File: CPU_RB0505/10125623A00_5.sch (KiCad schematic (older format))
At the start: 46 parts, among them IC21 LT1236ACS8-5, IC23 LT1236ACS8-10, IC24 STM809LWX, IC25 STM809LWX, IC26 LF33CDT, IC29 TPS5430, IC36 STM809TWX, T10 FZT953, T11 FZT953, T12 FZT953

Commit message: Sheet 5 made on grid and "pretty"
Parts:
- removed C46, C74, C80, C83: 100nF, 10125623A00:C0805, symbol 10125623A00-eagle-import:C0805
- removed C47: 220pF, 10125623A00:C0805, symbol 10125623A00-eagle-import:C0805
- removed D11: STPS340U, 10125623A00:SOT23DIO, symbol 10125623A00-eagle-import:BAT54
- removed IC29: TPS5430, 10125623A00:SO8POWERPAD, symbol 10125623A00-eagle-import:TPS5430DDA
- removed L2: 33µH, 10125623A00:WE-TPC-MH, symbol 10125623A00-eagle-import:WE-TPC-MH
- removed L30: 7427504, 10125623A00:PERL-FER, symbol 10125623A00-eagle-import:7427504
- removed R36: 75K, 10125623A00:R0805, symbol 10125623A00-eagle-import:R0805
- removed R41: 4.7K, 10125623A00:R1206, symbol 10125623A00-eagle-import:R1206
- removed T12: FZT953, 10125623A00:SOT223, symbol 10125623A00-eagle-import:BCP51
- added C117: 10µF, 10125623A00:TANTALB, symbol cpu-board:TANTALB
- added C80 (x2): 100nF, 10125623A00:C0805, symbol 10125623A00-eagle-import:C0805
- added C81: 10uF, 10125623A00:TANTALD, symbol cpu-board:TANTALD
- added D11 (x2): STPS340U, 10125623A00:SOT23DIO, symbol 10125623A00-eagle-import:BAT54
- added IC29 (x2): TPS5430, 10125623A00:SO8POWERPAD, symbol 10125623A00-eagle-import:TPS5430DDA
- added L2 (x2): 33µH, 10125623A00:WE-TPC-MH, symbol 10125623A00-eagle-import:WE-TPC-MH
- added T12 (x2): FZT953, 10125623A00:SOT223, symbol 10125623A00-eagle-import:BCP51
- C106: symbol 10125623A00-eagle-import:CHCMS_D8 -> cpu-board:CHCMS_D8
- C108, C92: symbol 10125623A00-eagle-import:TANTALB -> cpu-board:TANTALB
- C21, C88: symbol 10125623A00-eagle-import:MV100?F50V -> cpu-board:MV100?F50V
- C85: symbol 10125623A00-eagle-import:TANTALD -> cpu-board:TANTALD
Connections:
- wire segments 181 -> 180
- no-connect marks 0 -> 3

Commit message: Combined all symbols into one project library
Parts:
- C105, C107, C79, C80, C82, C90, C91, C97: symbol 10125623A00-eagle-import:C0805 -> cpu-board:C0805
- C117: symbol 10125623A00-eagle-import:TANTALB -> cpu-board:TANTALB
- C81: symbol 10125623A00-eagle-import:TANTALD -> cpu-board:TANTALD
- D11: symbol 10125623A00-eagle-import:BAT54 -> cpu-board:BAT54
- D4: symbol 10125623A00-eagle-import:ICTE5 -> cpu-board:ICTE5
- D7: symbol 10125623A00-eagle-import:PRLL5819 -> cpu-board:PRLL5819
- FU2: symbol 10125623A00-eagle-import:SLOBLO -> cpu-board:SLOBLO
- IC21, IC23: symbol 10125623A00-eagle-import:LT1236 -> cpu-board:LT1236
- IC24, IC25, IC36: symbol 10125623A00-eagle-import:STM809 -> cpu-board:STM809
- IC26: symbol 10125623A00-eagle-import:LF33CDT -> cpu-board:LF33CDT
- IC29: symbol 10125623A00-eagle-import:TPS5430DDA -> cpu-board:TPS5430DDA
- JP9: symbol 10125623A00-eagle-import:JUMP_0U -> cpu-board:JUMP_0U
- L2: symbol 10125623A00-eagle-import:WE-TPC-MH -> cpu-board:WE-TPC-MH
- R35, R40, R44, R66, R67, R71, R73: symbol 10125623A00-eagle-import:R0805 -> cpu-board:R0805
- T10, T11, T12: symbol 10125623A00-eagle-import:BCP51 -> cpu-board:BCP51
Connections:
- wire segments 180 -> 177
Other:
- moved on the sheet: C117

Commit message: Corrected merge errors on sheet 5
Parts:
- removed C117 (x2): 10µF, 10125623A00:TANTALB, symbol cpu-board:TANTALB
- removed C80 (x2): 100nF, 10125623A00:C0805, symbol cpu-board:C0805
- removed C81 (x2): 10uF, 10125623A00:TANTALD, symbol cpu-board:TANTALD
- removed D11 (x2): STPS340U, 10125623A00:SOT23DIO, symbol cpu-board:BAT54
- removed IC29 (x2): TPS5430, 10125623A00:SO8POWERPAD, symbol cpu-board:TPS5430DDA
- removed L2 (x2): 33µH, 10125623A00:WE-TPC-MH, symbol cpu-board:WE-TPC-MH
- removed T12 (x2): FZT953, 10125623A00:SOT223, symbol cpu-board:BCP51
- added 1: CART_A3, symbol cpu-board:CART_A3
- added C117: 10µF, 10125623A00:TANTALB, symbol cpu-board:TANTALB
- added C46, C74, C80, C83: 100nF, 10125623A00:C0805, symbol cpu-board:C0805
- added C47: 220pF, 10125623A00:C0805, symbol cpu-board:C0805
- added C81: 10uF, 10125623A00:TANTALD, symbol cpu-board:TANTALD
- added D11: STPS340U, 10125623A00:SOT23DIO, symbol cpu-board:BAT54
- added IC29: TPS5430, 10125623A00:SO8POWERPAD, symbol cpu-board:TPS5430DDA
- added L2: 33µH, 10125623A00:WE-TPC-MH, symbol cpu-board:WE-TPC-MH
- added L30: 7427504, 10125623A00:PERL-FER, symbol cpu-board:7427504
- added R36: 75K, 10125623A00:R0805, symbol cpu-board:R0805
- added R41: 4.7K, 10125623A00:R1206, symbol cpu-board:R1206
- added T12: FZT953, 10125623A00:SOT223, symbol cpu-board:BCP51
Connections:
- net labels removed: CART_A3, PORT, PORT_LONG
- wire segments 177 -> 178
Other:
- moved on the sheet: C117, C21, IC21, IC23

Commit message: Sheet 5 labels converted to hier.
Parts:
- removed 1: CART_A3, symbol cpu-board:CART_A3
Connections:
- net +10VREF: no longer names the net of C83.2, C85.+, IC23.6 (OUT), T12.2 (C), T12.4 (C2)
- net +10VREF: no longer R66.1
- net +3,3V: no longer names the net of C90.2, C92.+, IC26.OUTPUT (VOUT)
- net +3,3V: no longer IC36.3 (VCC)
- net +5VREF: no longer names the net of C80.2, C81.+, IC21.6 (OUT), T11.2 (C), T11.4 (C2)
- net +5VREF: no longer IC24.3 (VCC)
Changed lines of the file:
@@
 Text Notes 13825 11025 0    170  ~ 0
 10125623
-Text GLabel 4175 2250 2    56   Output ~ 0
-+5VREF
-Text GLabel 4175 4650 2    56   Output ~ 0
-+10VREF
-Text GLabel 4250 6400 2    56   Output ~ 0
-+3,3V
-Text GLabel 7850 3900 0    56   Input ~ 0
-+10VREF
-Text GLabel 7850 6250 0    70   Input ~ 0
-+3,3V
-Text GLabel 9825 2300 2    56   Output ~ 0
+Text HLabel 9825 2300 2    56   Output ~ 0
 +5VREF-FAILURE
-Text GLabel 9825 4575 2    56   Output ~ 0
+Text HLabel 9825 4575 2    56   Output ~ 0
 +10VREF-FAILURE
-Text GLabel 9825 6925 2    56   Output ~ 0
+Text HLabel 9825 6925 2    56   Output ~ 0
 +3,3V-FAILURE
-Text GLabel 15250 2500 2    56   Output ~ 0
+Text HLabel 15250 2500 2    56   Output ~ 0
 MES-24V
 $Comp
@@
 Connection ~ 3925 2250
 Wire Wire Line
-	3925 2250 4175 2250
-Wire Wire Line
 	3925 2375 3925 2250
 Wire Wire Line
@@
 Connection ~ 3925 4650
 Wire Wire Line
-	3925 4650 4175 4650
-Wire Wire Line
 	3925 4775 3925 4650
 Wire Wire Line
@@
 Wire Wire Line
 	3975 6250 3975 6400
-Connection ~ 3975 6400
-Wire Wire Line
-	3975 6400 4250 6400
 Wire Wire Line
 	1700 9875 1700 10325
@@
 Wire Wire Line
 	7950 3900 7850 3900
-Text GLabel 7850 1625 0    56   Input ~ 0
-+5VREF
-Wire Wire Line
-	7850 1625 8750 1625
-Wire Wire Line
-	8750 1625 8750 1800
+Wire Wire Line
+	7850 1750 8750 1750
+Wire Wire Line
+	8750 1750 8750 1800
 Wire Wire Line
 	9450 2300 9825 2300
@@
 	12700 1975 12975 1975
 $Comp
-L cpu-board:CART_A3 1
-U 1 1 5EBB773C
-P 925 11100
-F 0 "1" H 975 11150 50  0001 C CNN
-F 1 "CART_A3" H 925 11100 50  0001 C CNN
-F 2 "" H 925 11100 50  0001 C CNN
-F 3 "" H 925 11100 50  0001 C CNN
-	1    925  11100
-	1    0    0    -1
-$EndComp
+L cpu-board:+3,3V #U$?
+U 1 1 5E9E0DC3
+P 7850 6300
+AR Path="/5E9E0DC3" Ref="#U$?"  Part="1"
+AR Path="/5E92540F/5E9E0DC3" Ref="#U$?"  Part="1"
+F 0 "#U$?" H 7850 6300 50  0001 C CNN
+F 1 "+3,3V" H 7750 6512 59  0000 L BNN
+F 2 "" H 7850 6300 50  0001 C CNN
+F 3 "" H 7850 6300 50  0001 C CNN
+	1    7850 6300
+	1    0    0    -1
+$EndComp
+Wire Wire Line
+	7850 6200 7850 6250
+$Comp
+L cpu-board:+10VREF #U$?
+U 1 1 5E9E8B84
+P 7850 3800
+AR Path="/5E9E8B84" Ref="#U$?"  Part="1"
+AR Path="/5E92540F/5E9E8B84" Ref="#U$?"  Part="1"
+F 0 "#U$?" H 7850 3800 50  0001 C CNN
+F 1 "+10VREF" H 7675 3625 59  0000 L BNN
+F 2 "" H 7850 3800 50  0001 C CNN
+F 3 "" H 7850 3800 50  0001 C CNN
+	1    7850 3800
+	-1   0    0    1
+$EndComp
+$Comp
+L cpu-board:+5VREF #U$?
+U 1 1 5E9E93B2
+P 7850 1625
+AR Path="/5E9E93B2" Ref="#U$?"  Part="1"
+AR Path="/5E92540F/5E9E93B2" Ref="#U$?"  Part="1"
+F 0 "#U$?" H 7850 1625 50  0001 C CNN
+F 1 "+5VREF" H 7675 1537 59  0000 L BNN
+F 2 "" H 7850 1625 50  0001 C CNN
+F 3 "" H 7850 1625 50  0001 C CNN
+	1    7850 1625
+	-1   0    0    1
+$EndComp
+Wire Wire Line
+	7850 1725 7850 1750
+Wire Wire Line
+	7850 3800 7850 3900
 $EndSCHEMATC

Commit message: Added sheet 5 "CART_A3" for visual consistancy
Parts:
- added CART_A3_5: CART_A3, symbol cpu-board:CART_A3
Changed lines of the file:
@@
 Wire Wire Line
 	7850 3800 7850 3900
+$Comp
+L cpu-board:CART_A3 CART_A3_5
+U 1 1 602E287D
+P 925 11100
+F 0 "CART_A3_5" H 975 11150 50  0001 C CNN
+F 1 "CART_A3" H 925 11100 50  0001 C CNN
+F 2 "" H 925 11100 50  0001 C CNN
+F 3 "" H 925 11100 50  0001 C CNN
+	1    925  11100
+	1    0    0    -1
+$EndComp
 $EndSCHEMATC

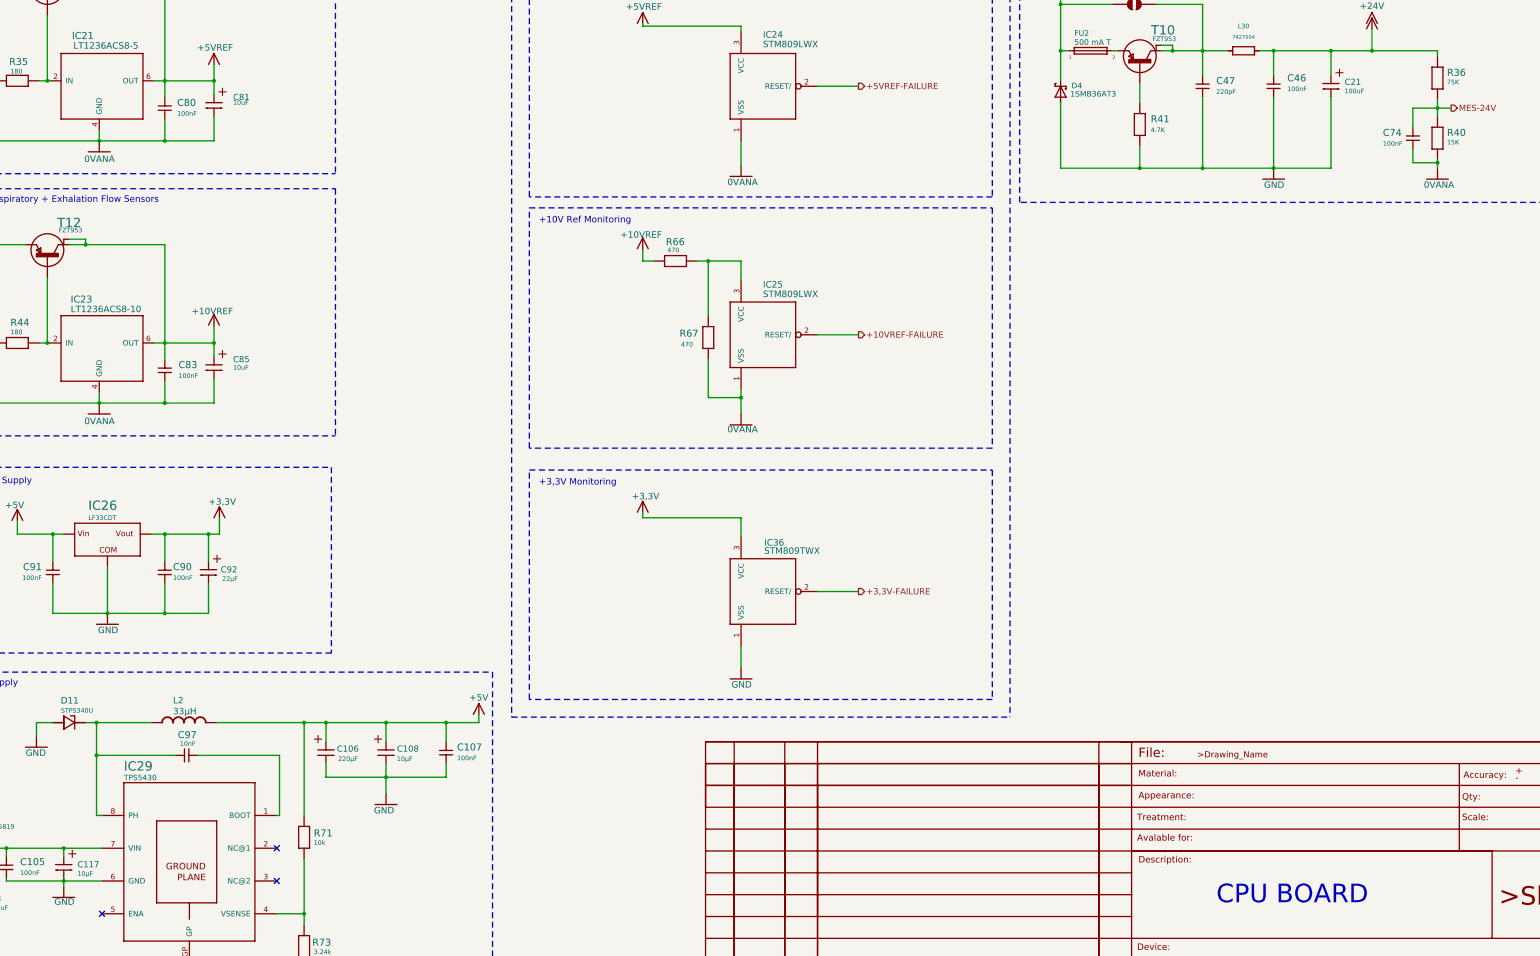
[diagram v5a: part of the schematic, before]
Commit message: Standardized value suffixes to "k" and "u"
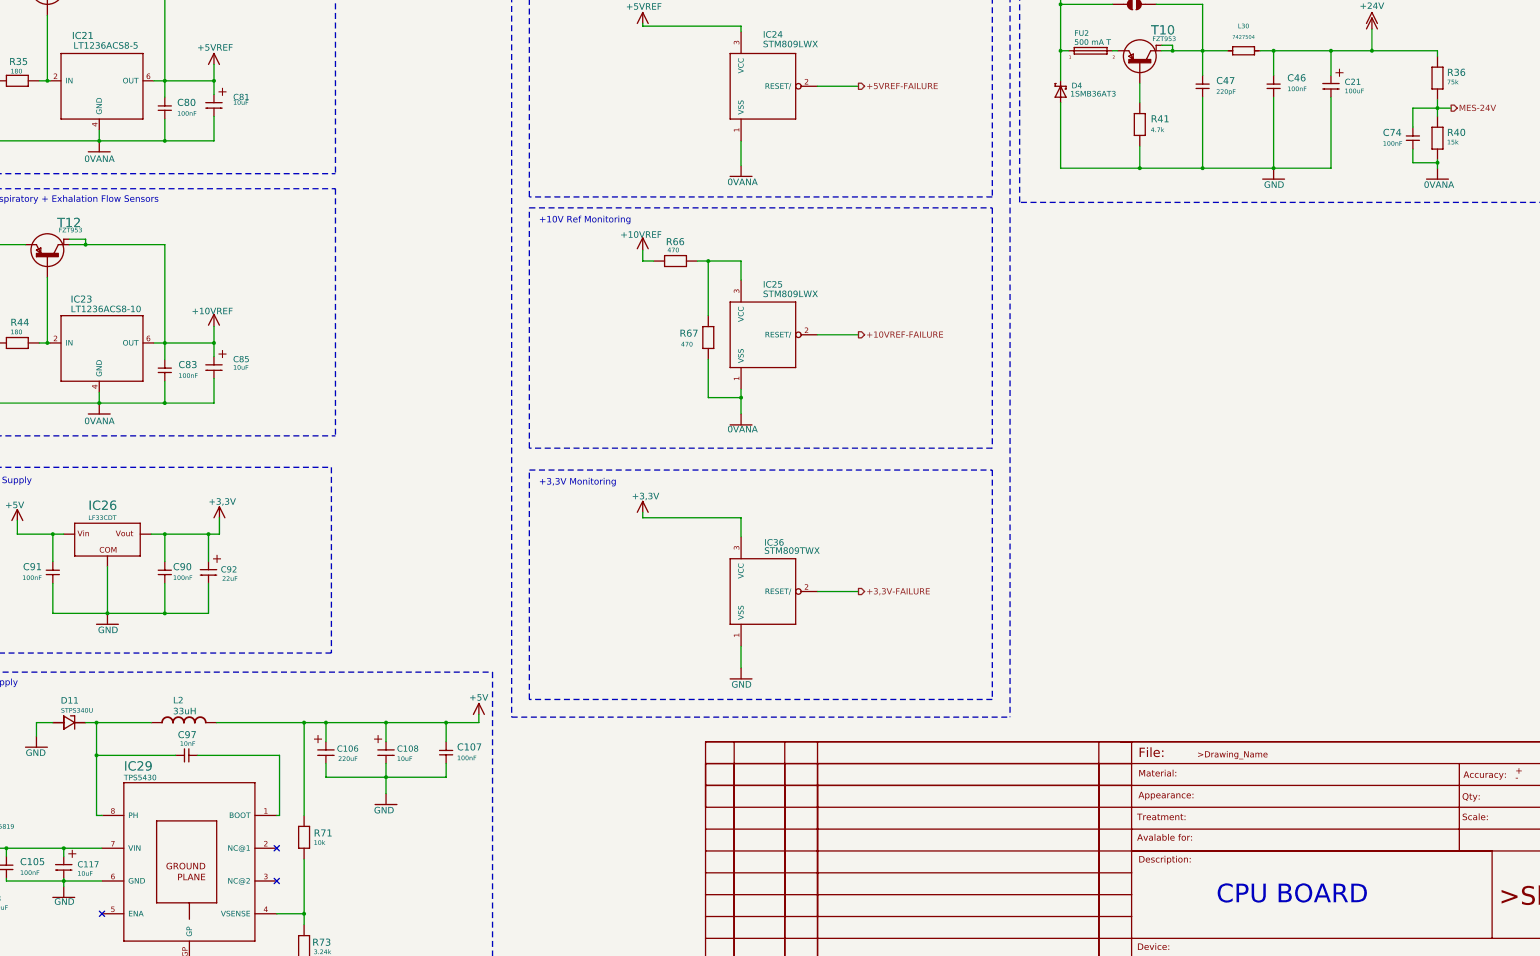
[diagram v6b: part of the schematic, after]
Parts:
- C106: value 220µF -> 220uF
- C108, C117: value 10µF -> 10uF
- C92: value 22µF -> 22uF
- L2: value 33µH -> 33uH
- R36: value 75K -> 75k
- R40: value 15K -> 15k
- R41: value 4.7K -> 4.7k
- R67: value 470 -> 470
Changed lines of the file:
@@
 AR Path="/5E92540F/2547CA40" Ref="R67"  Part="1"
 F 0 "R67" V 8450 4863 64  0000 R TNN
-F 1 "470 " V 8363 4850 42  0000 R TNN
+F 1 "470" V 8363 4850 42  0000 R TNN
 F 2 "10125623A00:R0805" H 8450 4600 50  0001 C CNN
 F 3 "" H 8450 4600 50  0001 C CNN
@@
 AR Path="/5E92540F/7FF0BFE4" Ref="R40"  Part="1"
 F 0 "R40" V 15112 2862 64  0000 L BNN
-F 1 "15K" V 15187 2862 42  0000 L BNN
+F 1 "15k" V 15187 2862 42  0000 L BNN
 F 2 "10125623A00:R0805" H 15125 2775 50  0001 C CNN
 F 3 "" H 15125 2775 50  0001 C CNN
@@
 AR Path="/5E92540F/86B7B564" Ref="L2"  Part="1"
 F 0 "L2" H 3750 8363 59  0000 R TNN
-F 1 "33µH" H 3750 8263 59  0000 R TNN
+F 1 "33uH" H 3750 8263 59  0000 R TNN
 F 2 "10125623A00:WE-TPC-MH" H 3650 8125 50  0001 C CNN
 F 3 "" H 3650 8125 50  0001 C CNN
@@
 AR Path="/5E92540F/939B92B5" Ref="C92"  Part="1"
 F 0 "C92" H 3987 6743 56  0000 L BNN
-F 1 "22µF" H 4000 6668 42  0000 L BNN
+F 1 "22uF" H 4000 6668 42  0000 L BNN
 F 2 "10125623A00:TANTALB" H 3875 6750 50  0001 C CNN
 F 3 "" H 3875 6750 50  0001 C CNN
@@
 AR Path="/5E92540F/F8977F3B" Ref="C106"  Part="1"
 F 0 "C106" H 4850 8468 56  0000 R TNN
-F 1 "220µF" H 4838 8368 42  0000 R TNN
+F 1 "220uF" H 4838 8368 42  0000 R TNN
 F 2 "10125623A00:CHCMS_D8" H 4950 8400 50  0001 C CNN
 F 3 "" H 4950 8400 50  0001 C CNN
@@
 AR Path="/5E92540F/1DA7F1EB" Ref="C108"  Part="1"
 F 0 "C108" H 5400 8468 56  0000 R TNN
-F 1 "10µF" H 5400 8368 42  0000 R TNN
+F 1 "10uF" H 5400 8368 42  0000 R TNN
 F 2 "10125623A00:TANTALB" H 5500 8400 50  0001 C CNN
 F 3 "" H 5500 8400 50  0001 C CNN
@@
 AR Path="/5E92540F/E481EE55" Ref="C117"  Part="1"
 F 0 "C117" H 2675 9443 56  0000 L BNN
-F 1 "10µF" H 2675 9368 42  0000 L BNN
+F 1 "10uF" H 2675 9368 42  0000 L BNN
 F 2 "10125623A00:TANTALB" H 2550 9450 50  0001 C CNN
 F 3 "" H 2550 9450 50  0001 C CNN
@@
 P 12400 2650
 F 0 "R41" V 12350 2750 64  0000 L CNN
-F 1 "4.7K" V 12450 2750 42  0000 L CNN
+F 1 "4.7k" V 12450 2750 42  0000 L CNN
 F 2 "10125623A00:R1206" H 12400 2650 50  0001 C CNN
 F 3 "" H 12400 2650 50  0001 C CNN
@@
 AR Path="/5E92540F/5EB4CA51" Ref="R36"  Part="1"
 F 0 "R36" V 15112 2312 64  0000 L BNN
-F 1 "75K" V 15187 2312 42  0000 L BNN
+F 1 "75k" V 15187 2312 42  0000 L BNN
 F 2 "10125623A00:R0805" H 15125 2225 50  0001 C CNN
 F 3 "" H 15125 2225 50  0001 C CNN

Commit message: Updated to 'default.kicad_wks' - deleted sheet symbol - general cleanup
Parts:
- removed CART_A3_5: CART_A3, symbol cpu-board:CART_A3
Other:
- note removed: "10125623"
- note removed: "CPU BOARD"
- note removed: "RB0505"
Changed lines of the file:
@@
 encoding utf-8
 Sheet 6 8
-Title ""
+Title "RB0505 CPU Board"
 Date ""
 Rev ""
@@
 Text Notes 6900 5963 0    59   ~ 0
 +3,3V Monitoring
-Text Notes 8462 10638 0    59   ~ 0
+Text Notes 15762 10763 0    59   ~ 0
 A
-Text Notes 8700 10638 0    59   ~ 0
+Text Notes 16000 10763 0    59   ~ 0
 05/03/14
-Text Notes 9200 10650 0    59   ~ 0
+Text Notes 16500 10775 0    59   ~ 0
 JR
 Text Notes 11337 1088 0    56   ~ 0
 STARTING CURRENT PROTECTION
-Text Notes 13100 9800 0    170  ~ 0
-CPU BOARD
-Text Notes 13650 10550 0    170  ~ 0
-RB0505
-Text Notes 13825 11025 0    170  ~ 0
-10125623
 Text HLabel 9825 2300 2    56   Output ~ 0
 +5VREF-FAILURE
@@
 Wire Wire Line
 	7850 3800 7850 3900
-$Comp
-L cpu-board:CART_A3 CART_A3_5
-U 1 1 602E287D
-P 925 11100
-F 0 "CART_A3_5" H 975 11150 50  0001 C CNN
-F 1 "CART_A3" H 925 11100 50  0001 C CNN
-F 2 "" H 925 11100 50  0001 C CNN
-F 3 "" H 925 11100 50  0001 C CNN
-	1    925  11100
-	1    0    0    -1
-$EndComp
 $EndSCHEMATC
